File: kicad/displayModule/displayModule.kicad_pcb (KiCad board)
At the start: 2 copper layers, 13 parts, among them J1 Connector, Q1 2N7000, Q2 2N7000, Q3 2N7000, Q4 2N7000, Q5 2N7000, Q6 2N7000, U1 ATtiny85-20PU, U2 74HC595, U3 74HC595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

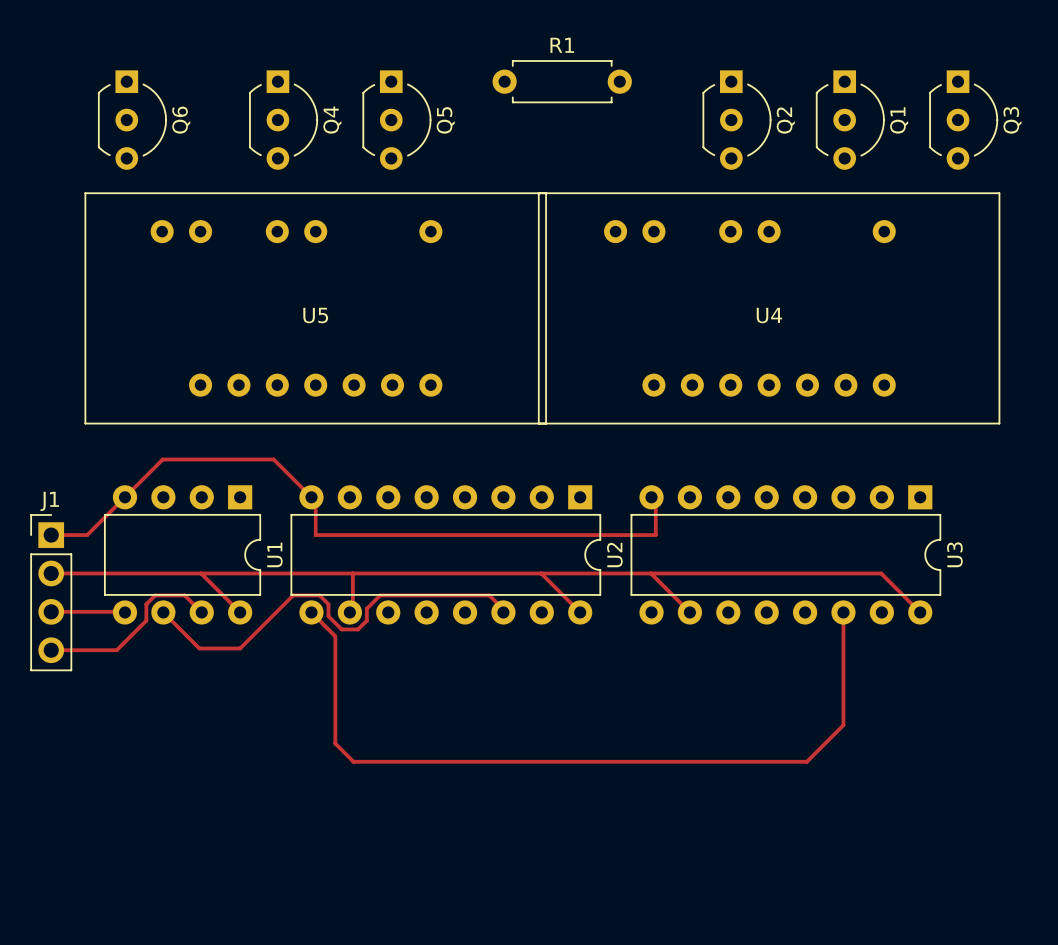
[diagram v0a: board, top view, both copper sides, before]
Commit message: Only activate squelch after AM transmission is picked up
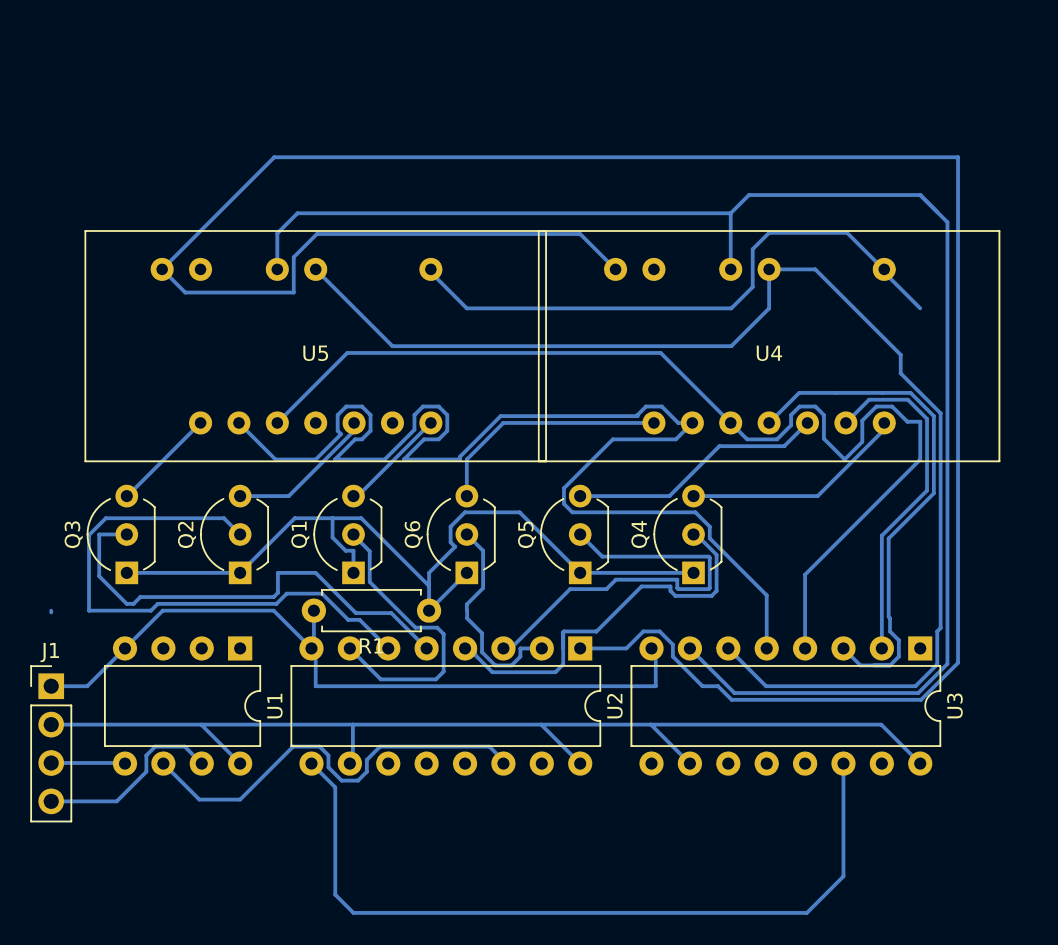
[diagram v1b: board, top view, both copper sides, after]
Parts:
- moved Q3 63.9 mm to (-720.0, 77.5), turned to 90 degrees
- moved Q1 46.0 mm to (-705.0, 77.5), turned to 90 degrees
- moved Q2 46.0 mm to (-712.5, 77.5), turned to 90 degrees
- moved Q4 42.6 mm to (-682.5, 77.5), turned to 90 degrees
- moved Q6 39.5 mm to (-697.5, 77.5), turned to 90 degrees
- moved R1 35.4 mm to (-700.0, 80.0), turned to 180 degrees
- moved Q5 34.8 mm to (-690.0, 77.5), turned to 90 degrees
- moved J1 10.0 mm to (-725.0, 85.0)
- moved U1 10.0 mm to (-712.5, 82.5)
- moved U2 10.0 mm to (-690.0, 82.5)
- moved U3 10.0 mm to (-667.5, 82.5)
- moved U4 2.50 mm to (-677.5, 62.5)
- moved U5 2.50 mm to (-707.5, 62.5)
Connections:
- U2 pad 2: Net-(Q4-Pad2) -> Net-(Q6-Pad2)
- U2 pad 4: Net-(Q6-Pad2) -> Net-(Q4-Pad2)
- U2 pad 5: Net-(Q1-Pad2) -> Net-(Q3-Pad2)
- U2 pad 7: Net-(Q3-Pad2) -> Net-(Q1-Pad2)
- U4 pad 1: Net-(Q1-Pad3) -> Net-(Q6-Pad3)
- U4 pad 5: Net-(Q2-Pad3) -> Net-(Q5-Pad3)
- U4 pad 7: Net-(Q3-Pad3) -> Net-(Q4-Pad3)
- U5 pad 1: Net-(Q4-Pad3) -> Net-(Q3-Pad3)
- U5 pad 5: Net-(Q5-Pad3) -> Net-(Q2-Pad3)
- U5 pad 7: Net-(Q6-Pad3) -> Net-(Q1-Pad3)
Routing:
- net Net-(U2-Pad1): track 0.00 -> 152.6 mm
- net Net-(U3-Pad7): track 0.00 -> 102.1 mm
- net Net-(U3-Pad6): track 0.00 -> 83.9 mm
- net Net-(U3-Pad5): track 0.00 -> 83.5 mm
- net Net-(U3-Pad4): track 0.00 -> 71.5 mm
- net Net-(Q1-Pad1): track 0.00 -> 55.9 mm
- net Net-(U3-Pad1): track 0.00 -> 39.3 mm
- net Net-(Q2-Pad2): track 0.00 -> 37.7 mm
- net Net-(U3-Pad3): track 0.00 -> 35.3 mm
- net Net-(Q3-Pad2): track 0.00 -> 30.9 mm
- net Net-(Q4-Pad2): track 0.00 -> 27.7 mm
- net Net-(Q5-Pad2): track 0.00 -> 27.4 mm
- net Net-(U3-Pad2): track 0.00 -> 23.3 mm
- net Net-(Q1-Pad2): track 0.00 -> 19.7 mm
- net Net-(Q5-Pad3): track 0.00 -> 17.0 mm
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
